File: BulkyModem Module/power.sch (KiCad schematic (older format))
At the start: 9 parts, among them J1 DC IN, K1 HK19F-DC, U2 74HCT04

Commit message: C64 UserPort adapter sketched out (preliminary layout)
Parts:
- D1: footprint (none) -> Diode_THT:D_DO-35_SOD27_P7.62mm_Horizontal
- JP1: footprint (none) -> Connector_PinHeader_2.54mm:PinHeader_1x02_P2.54mm_Vertical
- JP2: footprint Jumper:SolderJumper-3_P1.3mm_Open_RoundedPad1.0x1.5mm -> Jumper:SolderJumper-2_P1.3mm_Open_Pad1.0x1.5mm
- K1: footprint (none) -> HK19F-DC:HK19F-DC
- U2: footprint (none) -> Package_DIP:DIP-14_W7.62mm_Socket_LongPads
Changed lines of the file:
@@
 F 0 "K1" H 8150 3700 50  0000 L CNN
 F 1 "HK19F-DC" H 8150 3600 50  0000 L CNN
-F 2 "" H 8075 3775 50  0001 C CNN
+F 2 "HK19F-DC:HK19F-DC" H 8075 3775 50  0001 C CNN
 F 3 "" H 8075 3775 50  0001 C CNN
 	1    7225 3650
@@
 F 0 "D1" V 6800 3400 50  0000 L CNN
 F 1 "1n4148" V 6875 3300 50  0000 L CNN
-F 2 "" H 6875 3650 50  0001 C CNN
+F 2 "Diode_THT:D_DO-35_SOD27_P7.62mm_Horizontal" H 6875 3650 50  0001 C CNN
 F 3 "~" H 6875 3650 50  0001 C CNN
 	1    6875 3650
@@
 F 0 "JP2" H 7725 3361 31  0000 C CNN
 F 1 "BYPASS" H 7725 3299 31  0000 C CNN
-F 2 "Jumper:SolderJumper-3_P1.3mm_Open_RoundedPad1.0x1.5mm" H 7725 3200 50  0001 C CNN
+F 2 "Jumper:SolderJumper-2_P1.3mm_Open_Pad1.0x1.5mm" H 7725 3200 50  0001 C CNN
 F 3 "~" H 7725 3200 50  0001 C CNN
 	1    7725 3200
@@
 F 0 "JP1" V 7275 4650 50  0000 R CNN
 F 1 "PWR_SW" V 7200 4725 50  0000 R CNN
-F 2 "" H 7225 4375 50  0001 C CNN
+F 2 "Connector_PinHeader_2.54mm:PinHeader_1x02_P2.54mm_Vertical" H 7225 4375 50  0001 C CNN
 F 3 "~" H 7225 4375 50  0001 C CNN
 	1    7225 4375
@@
 F 0 "U2" H 4875 4075 50  0000 C CNN
 F 1 "74HCT04" H 4875 3975 50  0000 C CNN
-F 2 "" H 4875 4025 50  0001 C CNN
+F 2 "Package_DIP:DIP-14_W7.62mm_Socket_LongPads" H 4875 4025 50  0001 C CNN
 F 3 "https://assets.nexperia.com/documents/data-sheet/74HC_HCT04.pdf" H 4875 4025 50  0001 C CNN
 	7    4875 4025

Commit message: Add DCD
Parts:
- added C17, C18: 100nF, Capacitor_THT:C_Disc_D4.7mm_W2.5mm_P5.00mm, symbol Device:C_Small
- added J4: Conn_Power, BulkyModem:Conn_Power, symbol BulkyModem:Conn_Power
- J1: footprint Connectors:BARREL_JACK -> BulkyModem:BARREL_JACK
- SYM1: footprint BulkyMIDI-32:PWR_Specification -> BulkyModem:PWR_Specification
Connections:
- net +5V: now also C17.1, C18.1
- net GND: now also C17.2, C18.2, J4.2 (GND)
- net VIN: now also J4.1 (VCC)
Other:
- moved on the sheet: C1, C6, J1, U2G
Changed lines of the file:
@@
 L barrel_jack:barrel_9v J?
 U 1 1 63DAB478
-P 3050 4025
+P 1375 4000
 AR Path="/63DAB478" Ref="J?"  Part="1"
 AR Path="/63D786E4/63DAB478" Ref="J1"  Part="1"
-F 0 "J1" H 3129 4350 50  0000 C CNN
-F 1 "DC IN" H 3129 4259 50  0000 C CNN
-F 2 "Connectors:BARREL_JACK" H 3100 3985 50  0001 C CNN
-F 3 "~" H 3100 3985 50  0001 C CNN
-	1    3050 4025
+F 0 "J1" H 1454 4325 50  0000 C CNN
+F 1 "DC IN" H 1454 4234 50  0000 C CNN
+F 2 "BulkyModem:BARREL_JACK" H 1425 3960 50  0001 C CNN
+F 3 "~" H 1425 3960 50  0001 C CNN
+	1    1375 4000
 	1    0    0    -1
 $EndComp
@@
 L power:GND #PWR?
 U 1 1 63DAB47E
-P 3725 4675
+P 2050 4650
 AR Path="/63DAB47E" Ref="#PWR?"  Part="1"
 AR Path="/63D786E4/63DAB47E" Ref="#PWR0108"  Part="1"
-F 0 "#PWR0108" H 3725 4425 50  0001 C CNN
-F 1 "GND" H 3730 4502 50  0000 C CNN
-F 2 "" H 3725 4675 50  0001 C CNN
-F 3 "" H 3725 4675 50  0001 C CNN
-	1    3725 4675
+F 0 "#PWR0108" H 2050 4400 50  0001 C CNN
+F 1 "GND" H 2055 4477 50  0000 C CNN
+F 2 "" H 2050 4650 50  0001 C CNN
+F 3 "" H 2050 4650 50  0001 C CNN
+	1    2050 4650
 	1    0    0    -1
 $EndComp
@@
 L Device:C_Small C?
 U 1 1 63DAB484
-P 4275 4025
+P 4825 4000
 AR Path="/63DAB484" Ref="C?"  Part="1"
 AR Path="/63D786E4/63DAB484" Ref="C6"  Part="1"
-F 0 "C6" H 4367 4071 50  0000 L CNN
-F 1 "100nF" H 4367 3980 50  0000 L CNN
-F 2 "Capacitor_THT:C_Disc_D4.7mm_W2.5mm_P5.00mm" H 4275 4025 50  0001 C CNN
-F 3 "~" H 4275 4025 50  0001 C CNN
-	1    4275 4025
-	1    0    0    -1
-$EndComp
-Wire Wire Line
-	3350 3925 3425 3925
-Wire Wire Line
-	3350 4125 3425 4125
+F 0 "C6" H 4917 4046 50  0000 L CNN
+F 1 "100nF" H 4917 3955 50  0000 L CNN
+F 2 "Capacitor_THT:C_Disc_D4.7mm_W2.5mm_P5.00mm" H 4825 4000 50  0001 C CNN
+F 3 "~" H 4825 4000 50  0001 C CNN
+	1    4825 4000
+	1    0    0    -1
+$EndComp
+Wire Wire Line
+	1675 3900 1750 3900
+Wire Wire Line
+	1675 4100 1750 4100
 $Comp
 L Device:CP1 C?
 U 1 1 63DAB48C
-P 3725 4025
+P 2050 4000
 AR Path="/63DAB48C" Ref="C?"  Part="1"
 AR Path="/63D786E4/63DAB48C" Ref="C1"  Part="1"
-F 0 "C1" H 3840 4071 50  0000 L CNN
-F 1 "470uF" H 3840 3980 50  0000 L CNN
-F 2 "Capacitor_THT:CP_Radial_D8.0mm_P3.50mm" H 3725 4025 50  0001 C CNN
-F 3 "~" H 3725 4025 50  0001 C CNN
-	1    3725 4025
+F 0 "C1" H 2165 4046 50  0000 L CNN
+F 1 "470uF" H 2165 3955 50  0000 L CNN
+F 2 "Capacitor_THT:CP_Radial_D8.0mm_P3.50mm" H 2050 4000 50  0001 C CNN
+F 3 "~" H 2050 4000 50  0001 C CNN
+	1    2050 4000
 	1    0    0    -1
 $EndComp
@@
 L power:+5V #PWR?
 U 1 1 63DAB492
-P 4275 3375
+P 3975 3350
 AR Path="/63DAB492" Ref="#PWR?"  Part="1"
 AR Path="/63D786E4/63DAB492" Ref="#PWR0110"  Part="1"
-F 0 "#PWR0110" H 4275 3225 50  0001 C CNN
-F 1 "+5V" H 4275 3515 50  0000 C CNN
-F 2 "" H 4275 3375 50  0000 C CNN
-F 3 "" H 4275 3375 50  0000 C CNN
-	1    4275 3375
-	1    0    0    -1
-$EndComp
-Wire Wire Line
-	4875 4600 4875 4525
+F 0 "#PWR0110" H 3975 3200 50  0001 C CNN
+F 1 "+5V" H 3975 3490 50  0000 C CNN
+F 2 "" H 3975 3350 50  0000 C CNN
+F 3 "" H 3975 3350 50  0000 C CNN
+	1    3975 3350
+	1    0    0    -1
+$EndComp
+Wire Wire Line
+	5375 4575 5375 4500
 $Comp
 L power:GND #PWR?
 U 1 1 63DAB499
-P 4875 4675
+P 5375 4650
 AR Path="/63DAB499" Ref="#PWR?"  Part="1"
 AR Path="/63D786E4/63DAB499" Ref="#PWR0133"  Part="1"
-F 0 "#PWR0133" H 4875 4425 50  0001 C CNN
-F 1 "GND" H 4880 4502 50  0000 C CNN
-F 2 "" H 4875 4675 50  0001 C CNN
-F 3 "" H 4875 4675 50  0001 C CNN
-	1    4875 4675
-	1    0    0    -1
-$EndComp
-Wire Wire Line
-	4275 4125 4275 4600
-Wire Wire Line
-	4275 3450 4275 3925
-Wire Wire Line
-	4875 3450 4875 3525
-Wire Wire Line
-	4275 3375 4275 3450
-Connection ~ 4275 3450
-Wire Wire Line
-	3350 4025 3425 4025
-Wire Wire Line
-	3425 4025 3425 4125
-Connection ~ 3425 4125
-Wire Wire Line
-	3725 3375 3725 3450
-Wire Wire Line
-	3725 3450 3425 3450
-Connection ~ 3725 3450
-Wire Wire Line
-	3425 3450 3425 3925
-Wire Wire Line
-	3725 3450 3725 3875
-Wire Wire Line
-	3725 4600 3425 4600
-Connection ~ 3725 4600
-Wire Wire Line
-	3725 4600 3725 4675
-Wire Wire Line
-	3425 4125 3425 4600
-Wire Wire Line
-	3725 4175 3725 4600
+F 0 "#PWR0133" H 5375 4400 50  0001 C CNN
+F 1 "GND" H 5380 4477 50  0000 C CNN
+F 2 "" H 5375 4650 50  0001 C CNN
+F 3 "" H 5375 4650 50  0001 C CNN
+	1    5375 4650
+	1    0    0    -1
+$EndComp
+Wire Wire Line
+	4825 4100 4825 4575
+Wire Wire Line
+	4825 3425 4825 3900
+Wire Wire Line
+	5375 3425 5375 3500
+Wire Wire Line
+	3975 3350 3975 3425
+Wire Wire Line
+	1675 4000 1750 4000
+Wire Wire Line
+	1750 4000 1750 4100
+Connection ~ 1750 4100
+Wire Wire Line
+	2050 3350 2050 3425
+Wire Wire Line
+	2050 3425 1750 3425
+Connection ~ 2050 3425
+Wire Wire Line
+	1750 3425 1750 3900
+Wire Wire Line
+	2050 3425 2050 3850
+Wire Wire Line
+	2050 4575 1750 4575
+Connection ~ 2050 4575
+Wire Wire Line
+	2050 4575 2050 4650
+Wire Wire Line
+	1750 4100 1750 4575
+Wire Wire Line
+	2050 4150 2050 4575
 $Comp
 L BulkyModem:DC_5V SYM?
 U 1 1 63DAB4B1
-P 3125 3525
+P 1450 3500
 AR Path="/63DAB4B1" Ref="SYM?"  Part="1"
 AR Path="/63D786E4/63DAB4B1" Ref="SYM1"  Part="1"
-F 0 "SYM1" H 3125 3746 50  0001 C CNN
-F 1 "DC_5V" H 3125 3654 50  0000 C CNN
-F 2 "BulkyMIDI-32:PWR_Specification" H 3000 3625 50  0001 C CNN
-F 3 "" H 3000 3625 50  0001 C CNN
-	1    3125 3525
+F 0 "SYM1" H 1450 3721 50  0001 C CNN
+F 1 "DC_5V" H 1450 3629 50  0000 C CNN
+F 2 "BulkyModem:PWR_Specification" H 1325 3600 50  0001 C CNN
+F 3 "" H 1325 3600 50  0001 C CNN
+	1    1450 3500
 	1    0    0    -1
 $EndComp
 Text Notes 2725 2725 0    50   ~ 0
 Power input and decoupling
-Wire Wire Line
-	4275 4600 4875 4600
 $Comp
 L barrel_jack:VIN #PWR?
 U 1 1 63DAB4BE
-P 3725 3375
+P 2050 3350
 AR Path="/63DAB4BE" Ref="#PWR?"  Part="1"
 AR Path="/63D786E4/63DAB4BE" Ref="#PWR0134"  Part="1"
-F 0 "#PWR0134" H 3725 3225 50  0001 C CNN
-F 1 "VIN" H 3742 3548 50  0000 C CNN
-F 2 "" H 3725 3375 50  0001 C CNN
-F 3 "" H 3725 3375 50  0001 C CNN
-	1    3725 3375
+F 0 "#PWR0134" H 2050 3200 50  0001 C CNN
+F 1 "VIN" H 2067 3523 50  0000 C CNN
+F 2 "" H 2050 3350 50  0001 C CNN
+F 3 "" H 2050 3350 50  0001 C CNN
+	1    2050 3350
 	1    0    0    -1
 $EndComp
@@
 L 74xx:74HCT04 U?
 U 7 1 63DAB4C4
-P 4875 4025
+P 5375 4000
 AR Path="/63DAB4C4" Ref="U?"  Part="7"
 AR Path="/63D786E4/63DAB4C4" Ref="U2"  Part="7"
-F 0 "U2" H 4875 4075 50  0000 C CNN
-F 1 "74HCT04" H 4875 3975 50  0000 C CNN
-F 2 "Package_DIP:DIP-14_W7.62mm_Socket_LongPads" H 4875 4025 50  0001 C CNN
-F 3 "https://assets.nexperia.com/documents/data-sheet/74HC_HCT04.pdf" H 4875 4025 50  0001 C CNN
-	7    4875 4025
-	1    0    0    -1
-$EndComp
-Wire Wire Line
-	4875 3450 4275 3450
-Wire Wire Line
-	4875 4675 4875 4600
-Connection ~ 4875 4600
+F 0 "U2" H 5375 4050 50  0000 C CNN
+F 1 "74HCT04" H 5375 3950 50  0000 C CNN
+F 2 "Package_DIP:DIP-14_W7.62mm_Socket_LongPads" H 5375 4000 50  0001 C CNN
+F 3 "https://assets.nexperia.com/documents/data-sheet/74HC_HCT04.pdf" H 5375 4000 50  0001 C CNN
+	7    5375 4000
+	1    0    0    -1
+$EndComp
+Wire Wire Line
+	5375 3425 4825 3425
+Wire Wire Line
+	5375 4650 5375 4575
+Connection ~ 5375 4575
 Text Notes 6325 2725 0    50   ~ 0
 Power switch uses a relay to provide power to the rest\nof the circuitry beyond the power section itself. This\nbypasses the kind of dodgy switches, as well as making\nan exciting clicking sound. Solder in the bypass jumper\nto skip installing relay, but you'll need to unplug the\ncable to turn it off.
 Wire Notes Line
 	5825 1725 5825 5550
+$Comp
+L BulkyModem:Conn_Power J4
+U 1 1 62DFBB40
+P 2800 3950
+F 0 "J4" H 3103 3946 50  0000 L CNN
+F 1 "Conn_Power" H 3103 3855 50  0000 L CNN
+F 2 "BulkyModem:Conn_Power" H 2800 3950 50  0001 C CNN
+F 3 "~" H 2800 3950 50  0001 C CNN
+	1    2800 3950
+	1    0    0    -1
+$EndComp
+Wire Wire Line
+	2050 3425 2525 3425
+Wire Wire Line
+	2525 3425 2525 3950
+Wire Wire Line
+	2525 3950 2600 3950
+Wire Wire Line
+	2600 4050 2525 4050
+Wire Wire Line
+	2525 4050 2525 4575
+Wire Wire Line
+	2525 4575 2050 4575
+$Comp
+L Device:C_Small C?
+U 1 1 6319B9B5
+P 4400 4000
+AR Path="/6319B9B5" Ref="C?"  Part="1"
+AR Path="/63D786E4/6319B9B5" Ref="C18"  Part="1"
+F 0 "C18" H 4492 4046 50  0000 L CNN
+F 1 "100nF" H 4492 3955 50  0000 L CNN
+F 2 "Capacitor_THT:C_Disc_D4.7mm_W2.5mm_P5.00mm" H 4400 4000 50  0001 C CNN
+F 3 "~" H 4400 4000 50  0001 C CNN
+	1    4400 4000
+	1    0    0    -1
+$EndComp
+Wire Wire Line
+	4400 4100 4400 4575
+Wire Wire Line
+	4400 3425 4400 3900
+$Comp
+L Device:C_Small C?
+U 1 1 6319CE6C
+P 3975 4000
+AR Path="/6319CE6C" Ref="C?"  Part="1"
+AR Path="/63D786E4/6319CE6C" Ref="C17"  Part="1"
+F 0 "C17" H 4067 4046 50  0000 L CNN
+F 1 "100nF" H 4067 3955 50  0000 L CNN
+F 2 "Capacitor_THT:C_Disc_D4.7mm_W2.5mm_P5.00mm" H 3975 4000 50  0001 C CNN
+F 3 "~" H 3975 4000 50  0001 C CNN
+	1    3975 4000
+	1    0    0    -1
+$EndComp
+Wire Wire Line
+	3975 4100 3975 4575
+Wire Wire Line
+	3975 3425 3975 3900
+Connection ~ 4825 3425
+Connection ~ 4825 4575
+Wire Wire Line
+	4825 4575 5375 4575
+Connection ~ 4400 3425
+Wire Wire Line
+	4400 3425 3975 3425
+Wire Wire Line
+	3975 4575 4400 4575
+Connection ~ 4400 4575
+Wire Wire Line
+	4400 4575 4825 4575
+Connection ~ 3975 3425
+Wire Wire Line
+	4400 3425 4825 3425
 $EndSCHEMATC

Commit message: Initial layout
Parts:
- added C19, C7: 100nF, Capacitor_THT:C_Disc_D4.7mm_W2.5mm_P5.00mm, symbol Device:C_Small
- added U5: 74HCT04, Package_DIP:DIP-14_W7.62mm_Socket_LongPads, symbol 74xx:74HCT04
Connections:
- net +5V: now also C19.1, C7.1, U5.14 (VCC)
- net GND: now also C19.2, C7.2, U5.11, U5.13, U5.3, U5.5, U5.7 (GND), U5.9
- no-connect marks 2 -> 7
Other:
- moved on the sheet: C1, C17, C18, C6, J1, J4, U2G

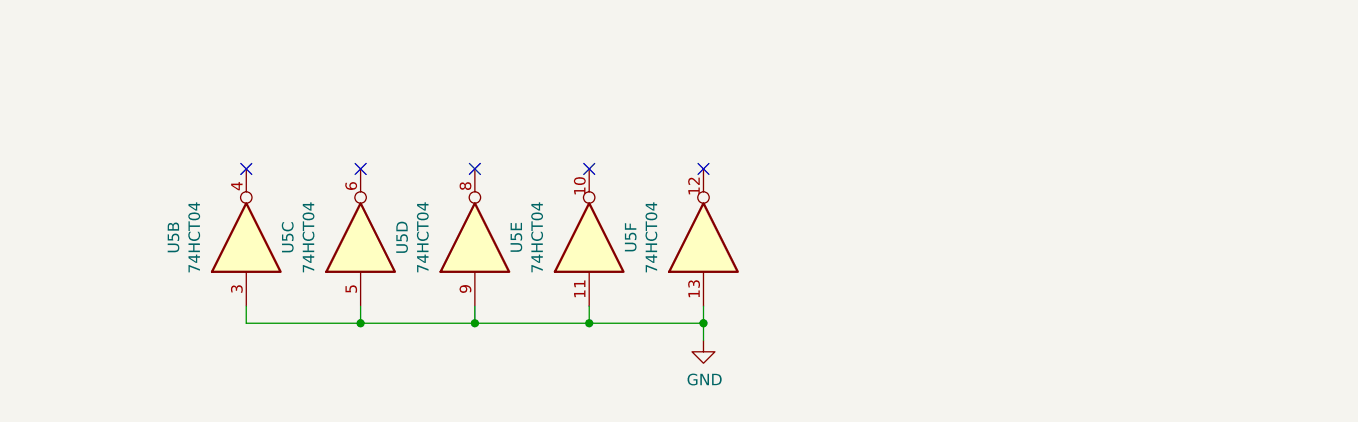
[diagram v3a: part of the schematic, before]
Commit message: Buffer RI and DCD with spare gates
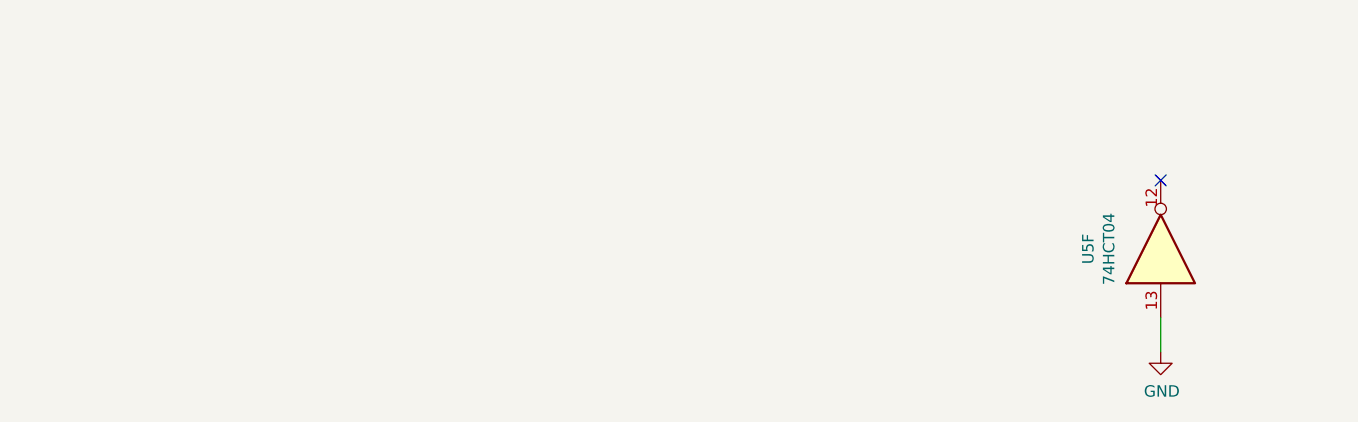
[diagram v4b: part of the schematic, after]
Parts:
- removed unit 2 of U5
- removed unit 3 of U5
- removed unit 5 of U5
- removed unit 4 of U5
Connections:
- no-connect marks 7 -> 3
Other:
- moved on the sheet: U5F
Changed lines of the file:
@@
-$Comp
-L 74xx:74HCT04 U?
-U 2 1 63272A2C
-P 2650 7000
-AR Path="/63272A2C" Ref="U?"  Part="1"
-AR Path="/6390AE73/63272A2C" Ref="U?"  Part="1"
-AR Path="/63D786E4/63272A2C" Ref="U5"  Part="2"
-F 0 "U5" H 2650 7317 50  0000 C CNN
-F 1 "74HCT04" H 2650 7226 50  0000 C CNN
-F 2 "Package_DIP:DIP-14_W7.62mm_Socket_LongPads" H 2650 7000 50  0001 C CNN
-F 3 "https://assets.nexperia.com/documents/data-sheet/74HC_HCT04.pdf" H 2650 7000 50  0001 C CNN
-	2    2650 7000
-	0    -1   -1   0
-$EndComp
-$Comp
-L 74xx:74HCT04 U?
-U 3 1 6327322F
-P 3150 7000
-AR Path="/6327322F" Ref="U?"  Part="1"
-AR Path="/6390AE73/6327322F" Ref="U?"  Part="1"
-AR Path="/63D786E4/6327322F" Ref="U5"  Part="3"
-F 0 "U5" H 3150 7317 50  0000 C CNN
-F 1 "74HCT04" H 3150 7226 50  0000 C CNN
-F 2 "Package_DIP:DIP-14_W7.62mm_Socket_LongPads" H 3150 7000 50  0001 C CNN
-F 3 "https://assets.nexperia.com/documents/data-sheet/74HC_HCT04.pdf" H 3150 7000 50  0001 C CNN
-	3    3150 7000
-	0    -1   -1   0
-$EndComp
-$Comp
-L 74xx:74HCT04 U?
-U 5 1 632737F0
-P 4150 7000
-AR Path="/632737F0" Ref="U?"  Part="1"
-AR Path="/6390AE73/632737F0" Ref="U?"  Part="1"
-AR Path="/63D786E4/632737F0" Ref="U5"  Part="5"
-F 0 "U5" H 4150 7317 50  0000 C CNN
-F 1 "74HCT04" H 4150 7226 50  0000 C CNN
-F 2 "Package_DIP:DIP-14_W7.62mm_Socket_LongPads" H 4150 7000 50  0001 C CNN
-F 3 "https://assets.nexperia.com/documents/data-sheet/74HC_HCT04.pdf" H 4150 7000 50  0001 C CNN
-	5    4150 7000
-	0    -1   -1   0
-$EndComp
-$Comp
-L 74xx:74HCT04 U?
-U 4 1 63273F9D
-P 3650 7000
-AR Path="/63273F9D" Ref="U?"  Part="1"
-AR Path="/6390AE73/63273F9D" Ref="U?"  Part="1"
-AR Path="/63D786E4/63273F9D" Ref="U5"  Part="4"
-F 0 "U5" H 3650 7317 50  0000 C CNN
-F 1 "74HCT04" H 3650 7226 50  0000 C CNN
-F 2 "Package_DIP:DIP-14_W7.62mm_Socket_LongPads" H 3650 7000 50  0001 C CNN
-F 3 "https://assets.nexperia.com/documents/data-sheet/74HC_HCT04.pdf" H 3650 7000 50  0001 C CNN
-	4    3650 7000
-	0    -1   -1   0
-$EndComp
 $Comp
 L 74xx:74HCT04 U?
 U 6 1 63275CC3
-P 4650 7000
+P 6650 7050
 AR Path="/63275CC3" Ref="U?"  Part="1"
 AR Path="/6390AE73/63275CC3" Ref="U?"  Part="1"
 AR Path="/63D786E4/63275CC3" Ref="U5"  Part="6"
-F 0 "U5" H 4650 7317 50  0000 C CNN
-F 1 "74HCT04" H 4650 7226 50  0000 C CNN
-F 2 "Package_DIP:DIP-14_W7.62mm_Socket_LongPads" H 4650 7000 50  0001 C CNN
-F 3 "https://assets.nexperia.com/documents/data-sheet/74HC_HCT04.pdf" H 4650 7000 50  0001 C CNN
-	6    4650 7000
+F 0 "U5" H 6650 7367 50  0000 C CNN
+F 1 "74HCT04" H 6650 7276 50  0000 C CNN
+F 2 "Package_DIP:DIP-14_W7.62mm_Socket_LongPads" H 6650 7050 50  0001 C CNN
+F 3 "https://assets.nexperia.com/documents/data-sheet/74HC_HCT04.pdf" H 6650 7050 50  0001 C CNN
+	6    6650 7050
 	0    -1   -1   0
 $EndComp
-NoConn ~ 2650 6700
-NoConn ~ 3150 6700
-NoConn ~ 3650 6700
-NoConn ~ 4150 6700
-NoConn ~ 4650 6700
-Wire Wire Line
-	4650 7300 4650 7375
-Wire Wire Line
-	4650 7375 4150 7375
-Wire Wire Line
-	4650 7375 4650 7450
-Connection ~ 4650 7375
+NoConn ~ 6650 6750
 $Comp
 L power:GND #PWR?
 U 1 1 632A80BC
-P 4650 7450
+P 6650 7500
 AR Path="/632A80BC" Ref="#PWR?"  Part="1"
 AR Path="/63D786E4/632A80BC" Ref="#PWR0105"  Part="1"
-F 0 "#PWR0105" H 4650 7200 50  0001 C CNN
-F 1 "GND" H 4655 7277 50  0000 C CNN
-F 2 "" H 4650 7450 50  0001 C CNN
-F 3 "" H 4650 7450 50  0001 C CNN
-	1    4650 7450
+F 0 "#PWR0105" H 6650 7250 50  0001 C CNN
+F 1 "GND" H 6655 7327 50  0000 C CNN
+F 2 "" H 6650 7500 50  0001 C CNN
+F 3 "" H 6650 7500 50  0001 C CNN
+	1    6650 7500
 	1    0    0    -1
 $EndComp
@@
 Connection ~ 1725 4325
 Wire Wire Line
-	2650 7300 2650 7375
-Wire Wire Line
-	3150 7300 3150 7375
-Connection ~ 3150 7375
-Wire Wire Line
-	3150 7375 2650 7375
-Wire Wire Line
-	3650 7300 3650 7375
-Connection ~ 3650 7375
-Wire Wire Line
-	3650 7375 3150 7375
-Wire Wire Line
-	4150 7300 4150 7375
-Connection ~ 4150 7375
-Wire Wire Line
-	4150 7375 3650 7375
+	6650 7350 6650 7500
 $EndSCHEMATC
